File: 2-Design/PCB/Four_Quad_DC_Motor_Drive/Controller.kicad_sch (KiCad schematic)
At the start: 0 parts

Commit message: Changed the driver schematic, and added some schematic symbols
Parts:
- added STM?: blue_pill, symbol ee463_symbol_library:blue_pill
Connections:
- new net +5V: STM?.18 (5V)
- new net GND: STM?.19 (G), STM?.21 (G), STM?.22 (G)
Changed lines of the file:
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@@
 (kicad_sch (version 20211123) (generator eeschema)
   (paper "A4")
+  (junction (at 116.84 57.15) (diameter 0) (color 0 0 0 0)
+  )
+  (wire (pts (xy 85.09 100.33) (xy 92.71 100.33))
+    (stroke (width 0) (type default) (color 0 0 0 0))
+  )
+  (wire (pts (xy 85.09 97.79) (xy 85.09 100.33))
+    (stroke (width 0) (type default) (color 0 0 0 0))
+  )
+  (wire (pts (xy 113.03 57.15) (xy 116.84 57.15))
+    (stroke (width 0) (type default) (color 0 0 0 0))
+  )
+  (wire (pts (xy 85.09 102.87) (xy 85.09 106.68))
+    (stroke (width 0) (type default) (color 0 0 0 0))
+  )
+  (wire (pts (xy 116.84 57.15) (xy 129.54 57.15))
+    (stroke (width 0) (type default) (color 0 0 0 0))
+  )
+  (wire (pts (xy 116.84 59.69) (xy 116.84 57.15))
+    (stroke (width 0) (type default) (color 0 0 0 0))
+  )
+  (wire (pts (xy 92.71 102.87) (xy 85.09 102.87))
+    (stroke (width 0) (type default) (color 0 0 0 0))
+  )
+  (wire (pts (xy 129.54 57.15) (xy 129.54 58.42))
+    (stroke (width 0) (type default) (color 0 0 0 0))
+  )
+  (wire (pts (xy 113.03 59.69) (xy 116.84 59.69))
+    (stroke (width 0) (type default) (color 0 0 0 0))
+  )
+  (symbol (lib_id "ee463_symbol_library:blue_pill") (at 102.87 80.01 0) (unit 1)
+    (in_bom yes) (on_board yes) (fields_autoplaced)
+    (property "Reference" "STM?" (id 0) (at 102.87 50.8 0))
+    (property "Value" "blue_pill" (id 1) (at 102.87 53.34 0))
+    (property "Footprint" "" (id 2) (at 105.41 80.01 0)
+      (effects (font (size 1.27 1.27)) hide)
+    )
+    (property "Datasheet" "" (id 3) (at 105.41 80.01 0)
+      (effects (font (size 1.27 1.27)) hide)
+    )
+    (pin "1")
+    (pin "10")
+    (pin "11")
+    (pin "12")
+    (pin "13")
+    (pin "14")
+    (pin "15")
+    (pin "16")
+    (pin "17")
+    (pin "18")
+    (pin "19")
+    (pin "2")
+    (pin "20")
+    (pin "21")
+    (pin "22")
+    (pin "23")
+    (pin "24")
+    (pin "25")
+    (pin "26")
+    (pin "27")
+    (pin "28")
+    (pin "29")
+    (pin "3")
+    (pin "30")
+    (pin "31")
+    (pin "32")
+    (pin "33")
+    (pin "34")
+    (pin "35")
+    (pin "36")
+    (pin "37")
+    (pin "38")
+    (pin "39")
+    (pin "4")
+    (pin "40")
+    (pin "5")
+    (pin "6")
+    (pin "7")
+    (pin "8")
+    (pin "9")
+  )
+  (symbol (lib_id "power:GND") (at 85.09 106.68 0) (unit 1)
+    (in_bom yes) (on_board yes) (fields_autoplaced)
+    (property "Reference" "#PWR?" (id 0) (at 85.09 113.03 0)
+      (effects (font (size 1.27 1.27)) hide)
+    )
+    (property "Value" "GND" (id 1) (at 85.09 111.76 0))
+    (property "Footprint" "" (id 2) (at 85.09 106.68 0)
+      (effects (font (size 1.27 1.27)) hide)
+    )
+    (property "Datasheet" "" (id 3) (at 85.09 106.68 0)
+      (effects (font (size 1.27 1.27)) hide)
+    )
+    (pin "1")
+  )
+  (symbol (lib_id "power:+5V") (at 85.09 97.79 0) (unit 1)
+    (in_bom yes) (on_board yes) (fields_autoplaced)
+    (property "Reference" "#PWR?" (id 0) (at 85.09 101.6 0)
+      (effects (font (size 1.27 1.27)) hide)
+    )
+    (property "Value" "+5V" (id 1) (at 85.09 92.71 0))
+    (property "Footprint" "" (id 2) (at 85.09 97.79 0)
+      (effects (font (size 1.27 1.27)) hide)
+    )
+    (property "Datasheet" "" (id 3) (at 85.09 97.79 0)
+      (effects (font (size 1.27 1.27)) hide)
+    )
+    (pin "1")
+  )
+  (symbol (lib_id "power:GND") (at 129.54 58.42 0) (unit 1)
+    (in_bom yes) (on_board yes) (fields_autoplaced)
+    (property "Reference" "#PWR?" (id 0) (at 129.54 64.77 0)
+      (effects (font (size 1.27 1.27)) hide)
+    )
+    (property "Value" "GND" (id 1) (at 129.54 63.5 0))
+    (property "Footprint" "" (id 2) (at 129.54 58.42 0)
+      (effects (font (size 1.27 1.27)) hide)
+    )
+    (property "Datasheet" "" (id 3) (at 129.54 58.42 0)
+      (effects (font (size 1.27 1.27)) hide)
+    )
+    (pin "1")
+  )
 )

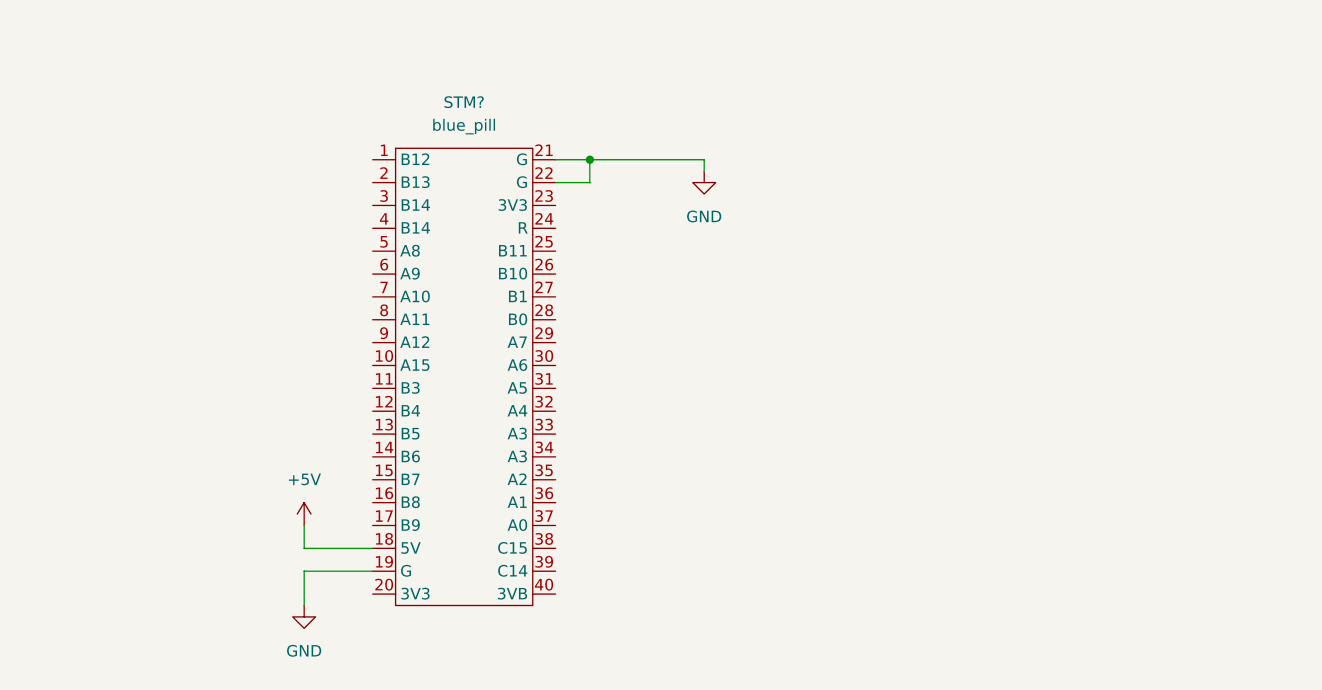
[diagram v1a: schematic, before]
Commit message: Added the label and gate drive resistances
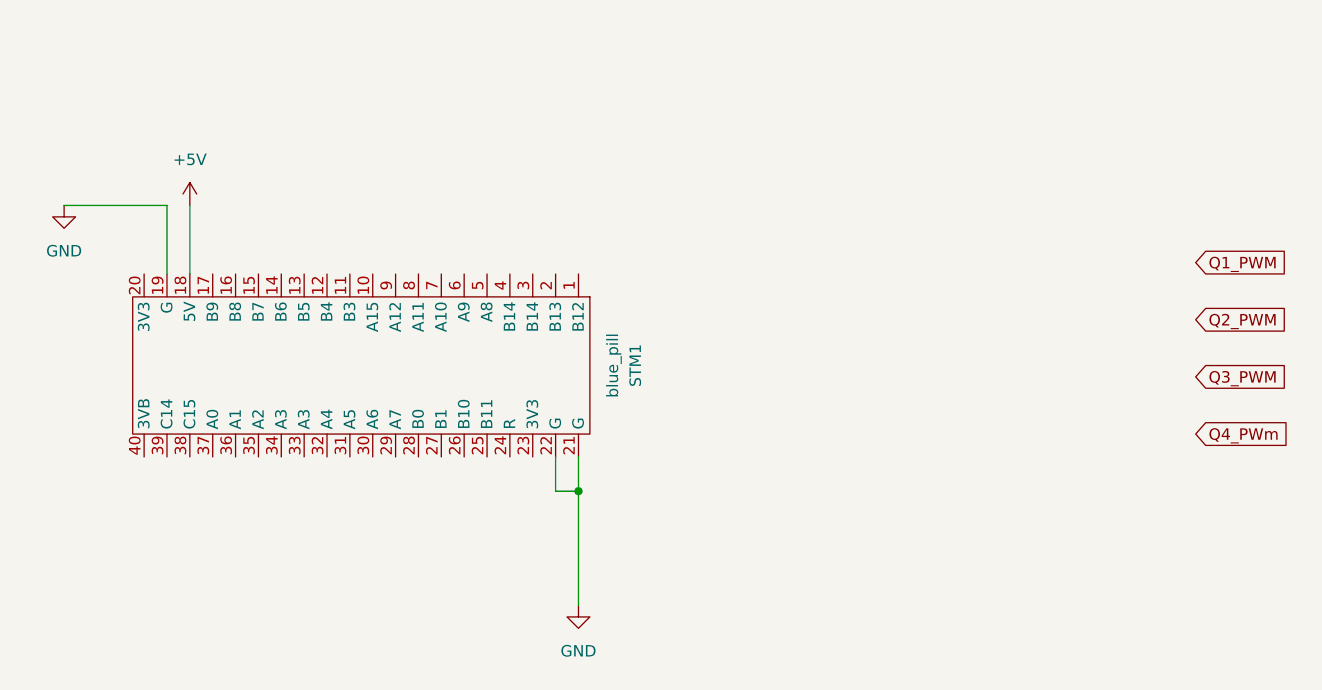
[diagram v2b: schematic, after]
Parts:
- gave numbers to parts that had none: 1
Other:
- moved on the sheet: STM1
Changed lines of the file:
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@@
 (kicad_sch (version 20211123) (generator eeschema)
   (paper "A4")
-  (junction (at 116.84 57.15) (diameter 0) (color 0 0 0 0)
+  (junction (at 115.57 93.98) (diameter 0) (color 0 0 0 0)
   )
-  (wire (pts (xy 85.09 100.33) (xy 92.71 100.33))
+  (wire (pts (xy 72.39 62.23) (xy 72.39 69.85))
     (stroke (width 0) (type default) (color 0 0 0 0))
   )
-  (wire (pts (xy 85.09 97.79) (xy 85.09 100.33))
+  (wire (pts (xy 115.57 90.17) (xy 115.57 93.98))
     (stroke (width 0) (type default) (color 0 0 0 0))
   )
-  (wire (pts (xy 113.03 57.15) (xy 116.84 57.15))
+  (wire (pts (xy 69.85 62.23) (xy 58.42 62.23))
     (stroke (width 0) (type default) (color 0 0 0 0))
   )
-  (wire (pts (xy 85.09 102.87) (xy 85.09 106.68))
+  (wire (pts (xy 115.57 93.98) (xy 115.57 106.68))
     (stroke (width 0) (type default) (color 0 0 0 0))
   )
-  (wire (pts (xy 116.84 57.15) (xy 129.54 57.15))
+  (wire (pts (xy 113.03 93.98) (xy 115.57 93.98))
     (stroke (width 0) (type default) (color 0 0 0 0))
   )
-  (wire (pts (xy 116.84 59.69) (xy 116.84 57.15))
+  (wire (pts (xy 69.85 69.85) (xy 69.85 62.23))
     (stroke (width 0) (type default) (color 0 0 0 0))
   )
-  (wire (pts (xy 92.71 102.87) (xy 85.09 102.87))
+  (wire (pts (xy 113.03 90.17) (xy 113.03 93.98))
     (stroke (width 0) (type default) (color 0 0 0 0))
   )
-  (wire (pts (xy 129.54 57.15) (xy 129.54 58.42))
-    (stroke (width 0) (type default) (color 0 0 0 0))
+  (global_label "Q1_PWM" (shape input) (at 184.15 68.58 0) (fields_autoplaced)
+    (effects (font (size 1.27 1.27)) (justify left))
+    (property "Intersheet References" "${INTERSHEET_REFS}" (id 0) (at 194.2436 68.5006 0)
+      (effects (font (size 1.27 1.27)) (justify left) hide)
+    )
   )
-  (wire (pts (xy 113.03 59.69) (xy 116.84 59.69))
-    (stroke (width 0) (type default) (color 0 0 0 0))
+  (global_label "Q2_PWM" (shape input) (at 184.15 74.93 0) (fields_autoplaced)
+    (effects (font (size 1.27 1.27)) (justify left))
+    (property "Intersheet References" "${INTERSHEET_REFS}" (id 0) (at 194.2436 74.8506 0)
+      (effects (font (size 1.27 1.27)) (justify left) hide)
+    )
   )
-  (symbol (lib_id "ee463_symbol_library:blue_pill") (at 102.87 80.01 0) (unit 1)
+  (global_label "Q3_PWM" (shape input) (at 184.15 81.28 0) (fields_autoplaced)
+    (effects (font (size 1.27 1.27)) (justify left))
+    (property "Intersheet References" "${INTERSHEET_REFS}" (id 0) (at 194.2436 81.2006 0)
+      (effects (font (size 1.27 1.27)) (justify left) hide)
+    )
+  )
+  (global_label "Q4_PWm" (shape input) (at 184.15 87.63 0) (fields_autoplaced)
+    (effects (font (size 1.27 1.27)) (justify left))
+    (property "Intersheet References" "${INTERSHEET_REFS}" (id 0) (at 194.4855 87.5506 0)
+      (effects (font (size 1.27 1.27)) (justify left) hide)
+    )
+  )
+  (symbol (lib_id "ee463_symbol_library:blue_pill") (at 92.71 80.01 270) (unit 1)
     (in_bom yes) (on_board yes) (fields_autoplaced)
-    (property "Reference" "STM?" (id 0) (at 102.87 50.8 0))
-    (property "Value" "blue_pill" (id 1) (at 102.87 53.34 0))
-    (property "Footprint" "" (id 2) (at 105.41 80.01 0)
+    (property "Reference" "STM1" (id 0) (at 121.92 80.01 0))
+    (property "Value" "blue_pill" (id 1) (at 119.38 80.01 0))
+    (property "Footprint" "" (id 2) (at 92.71 82.55 0)
       (effects (font (size 1.27 1.27)) hide)
     )
-    (property "Datasheet" "" (id 3) (at 105.41 80.01 0)
+    (property "Datasheet" "" (id 3) (at 92.71 82.55 0)
       (effects (font (size 1.27 1.27)) hide)
     )
@@
     (pin "9")
   )
-  (symbol (lib_id "power:GND") (at 85.09 106.68 0) (unit 1)
+  (symbol (lib_id "power:GND") (at 58.42 62.23 0) (unit 1)
     (in_bom yes) (on_board yes) (fields_autoplaced)
-    (property "Reference" "#PWR?" (id 0) (at 85.09 113.03 0)
+    (property "Reference" "#PWR09" (id 0) (at 58.42 68.58 0)
       (effects (font (size 1.27 1.27)) hide)
     )
-    (property "Value" "GND" (id 1) (at 85.09 111.76 0))
-    (property "Footprint" "" (id 2) (at 85.09 106.68 0)
+    (property "Value" "GND" (id 1) (at 58.42 67.31 0))
+    (property "Footprint" "" (id 2) (at 58.42 62.23 0)
       (effects (font (size 1.27 1.27)) hide)
     )
-    (property "Datasheet" "" (id 3) (at 85.09 106.68 0)
+    (property "Datasheet" "" (id 3) (at 58.42 62.23 0)
       (effects (font (size 1.27 1.27)) hide)
     )
     (pin "1")
   )
-  (symbol (lib_id "power:+5V") (at 85.09 97.79 0) (unit 1)
+  (symbol (lib_id "power:+5V") (at 72.39 62.23 0) (unit 1)
     (in_bom yes) (on_board yes) (fields_autoplaced)
-    (property "Reference" "#PWR?" (id 0) (at 85.09 101.6 0)
+    (property "Reference" "#PWR010" (id 0) (at 72.39 66.04 0)
       (effects (font (size 1.27 1.27)) hide)
     )
-    (property "Value" "+5V" (id 1) (at 85.09 92.71 0))
-    (property "Footprint" "" (id 2) (at 85.09 97.79 0)
+    (property "Value" "+5V" (id 1) (at 72.39 57.15 0))
+    (property "Footprint" "" (id 2) (at 72.39 62.23 0)
       (effects (font (size 1.27 1.27)) hide)
     )
-    (property "Datasheet" "" (id 3) (at 85.09 97.79 0)
+    (property "Datasheet" "" (id 3) (at 72.39 62.23 0)
       (effects (font (size 1.27 1.27)) hide)
     )
     (pin "1")
   )
-  (symbol (lib_id "power:GND") (at 129.54 58.42 0) (unit 1)
+  (symbol (lib_id "power:GND") (at 115.57 106.68 0) (unit 1)
     (in_bom yes) (on_board yes) (fields_autoplaced)
-    (property "Reference" "#PWR?" (id 0) (at 129.54 64.77 0)
+    (property "Reference" "#PWR011" (id 0) (at 115.57 113.03 0)
       (effects (font (size 1.27 1.27)) hide)
     )
-    (property "Value" "GND" (id 1) (at 129.54 63.5 0))
-    (property "Footprint" "" (id 2) (at 129.54 58.42 0)
+    (property "Value" "GND" (id 1) (at 115.57 111.76 0))
+    (property "Footprint" "" (id 2) (at 115.57 106.68 0)
       (effects (font (size 1.27 1.27)) hide)
     )
-    (property "Datasheet" "" (id 3) (at 129.54 58.42 0)
+    (property "Datasheet" "" (id 3) (at 115.57 106.68 0)
       (effects (font (size 1.27 1.27)) hide)
     )

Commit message: Gate driver changed, plus other rearrangements on the schematics
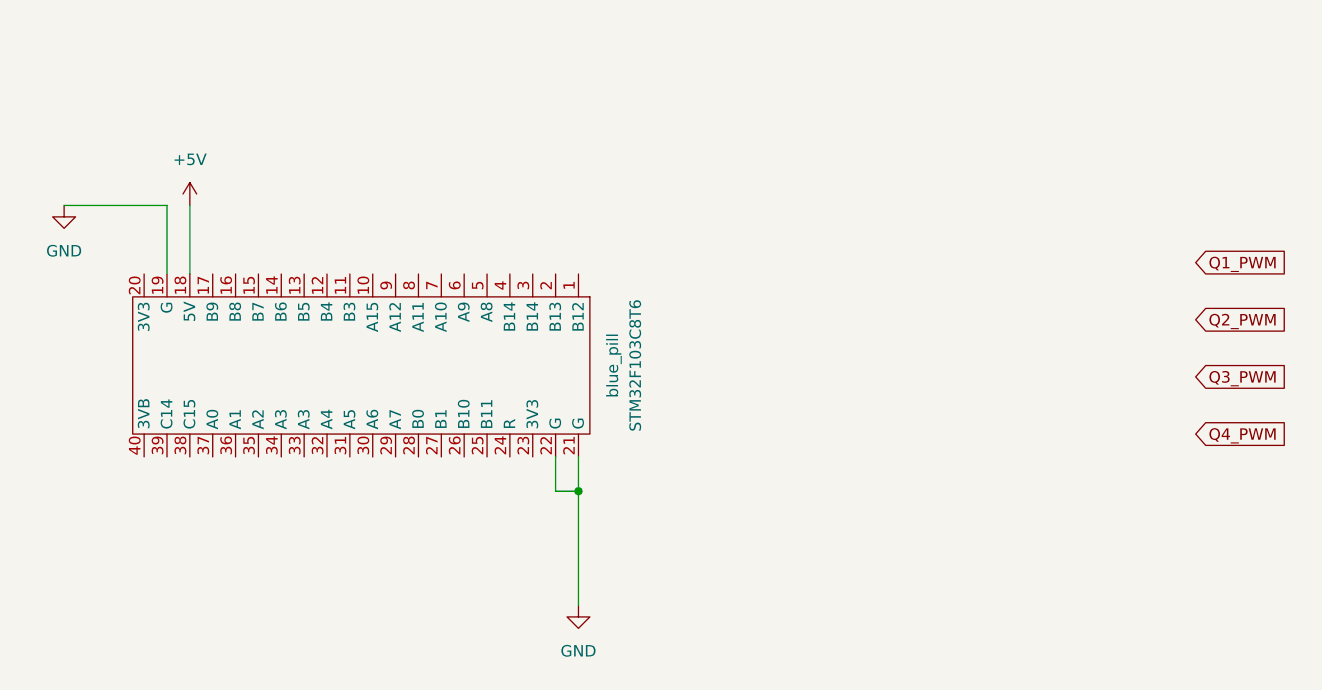
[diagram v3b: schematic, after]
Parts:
- STM32F103C8T6: renamed from STM1; footprint (none) -> ee463_footprint_lib:blue_pill
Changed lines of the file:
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@@
     )
   )
-  (global_label "Q4_PWm" (shape input) (at 184.15 87.63 0) (fields_autoplaced)
+  (global_label "Q4_PWM" (shape input) (at 184.15 87.63 0) (fields_autoplaced)
     (effects (font (size 1.27 1.27)) (justify left))
-    (property "Intersheet References" "${INTERSHEET_REFS}" (id 0) (at 194.4855 87.5506 0)
+    (property "Intersheet References" "${INTERSHEET_REFS}" (id 0) (at 194.2436 87.5506 0)
       (effects (font (size 1.27 1.27)) (justify left) hide)
     )
@@
   (symbol (lib_id "ee463_symbol_library:blue_pill") (at 92.71 80.01 270) (unit 1)
     (in_bom yes) (on_board yes) (fields_autoplaced)
-    (property "Reference" "STM1" (id 0) (at 121.92 80.01 0))
+    (property "Reference" "STM32F103C8T6" (id 0) (at 121.92 80.01 0))
     (property "Value" "blue_pill" (id 1) (at 119.38 80.01 0))
-    (property "Footprint" "" (id 2) (at 92.71 82.55 0)
+    (property "Footprint" "ee463_footprint_lib:blue_pill" (id 2) (at 92.71 82.55 0)
       (effects (font (size 1.27 1.27)) hide)
     )

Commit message: Random Checkpoint
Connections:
- net GND: now also STM32F103C8T6.17 (G), STM32F103C8T6.20 (G); no longer STM32F103C8T6.21 (G), STM32F103C8T6.22 (G)
- net Q1_PWM: now also STM32F103C8T6.5 (A8)
- net Q2_PWM: now also STM32F103C8T6.6 (A9)
- net Q3_PWM: now also STM32F103C8T6.7 (A10)
- net Q4_PWM: now also STM32F103C8T6.8 (A11)
- net Q5_PWM: now reaches STM32F103C8T6.25 (A0)
- net I_sense: now reaches STM32F103C8T6.26 (A1)
- net I_set: now reaches STM32F103C8T6.27 (A2)
- net Gen_mode: now reaches STM32F103C8T6.28 (A3)
- net Soft_st: now reaches STM32F103C8T6.29 (A4)
- net V_sense: now reaches STM32F103C8T6.30 (A5)
- net GPIO_INPUT_D: now reaches STM32F103C8T6.31 (A6)
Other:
- moved on the sheet: STM32F103C8T6
